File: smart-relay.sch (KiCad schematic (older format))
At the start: 16 parts, among them IC1 TMCS1101A4BQDR, J1 Screw_Terminal_01x03, J2 Conn_01x04, K1 G5LE-1, Q1 BSS138K, U1 OPAMP, U2 ATtiny85-20PU

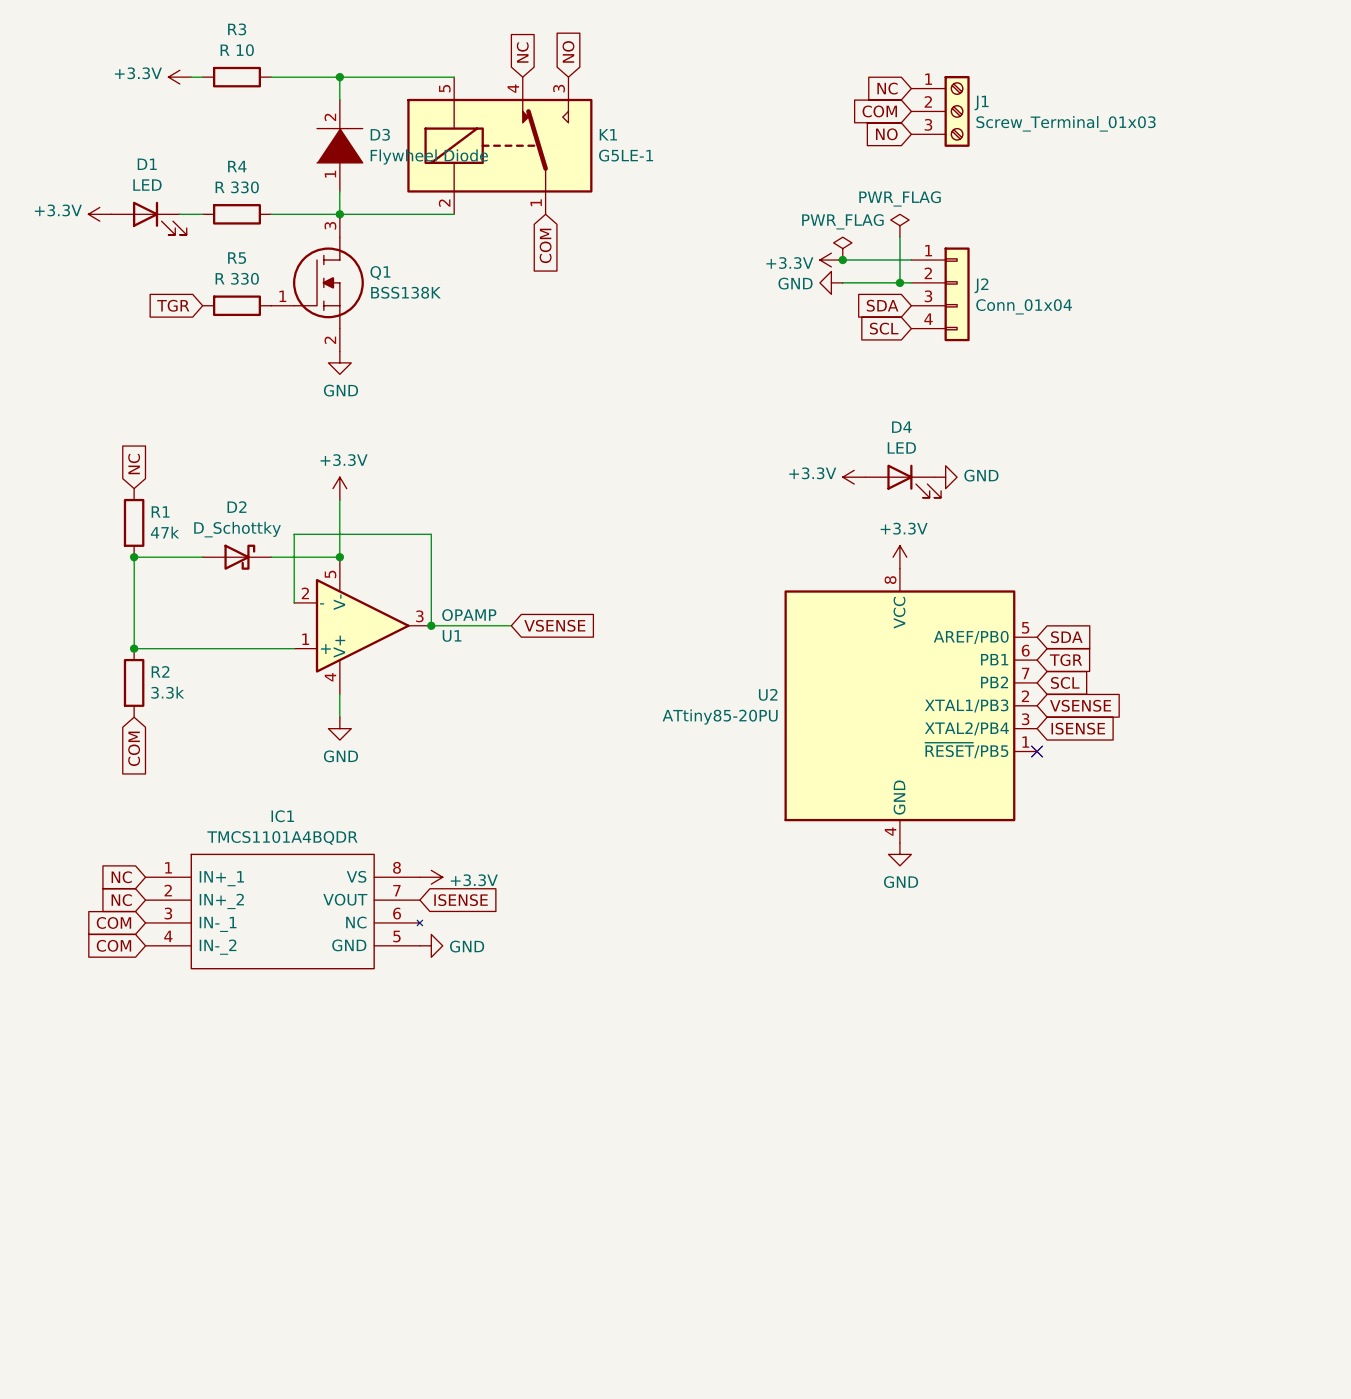
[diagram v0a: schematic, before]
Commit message: add decoupling cap and headers
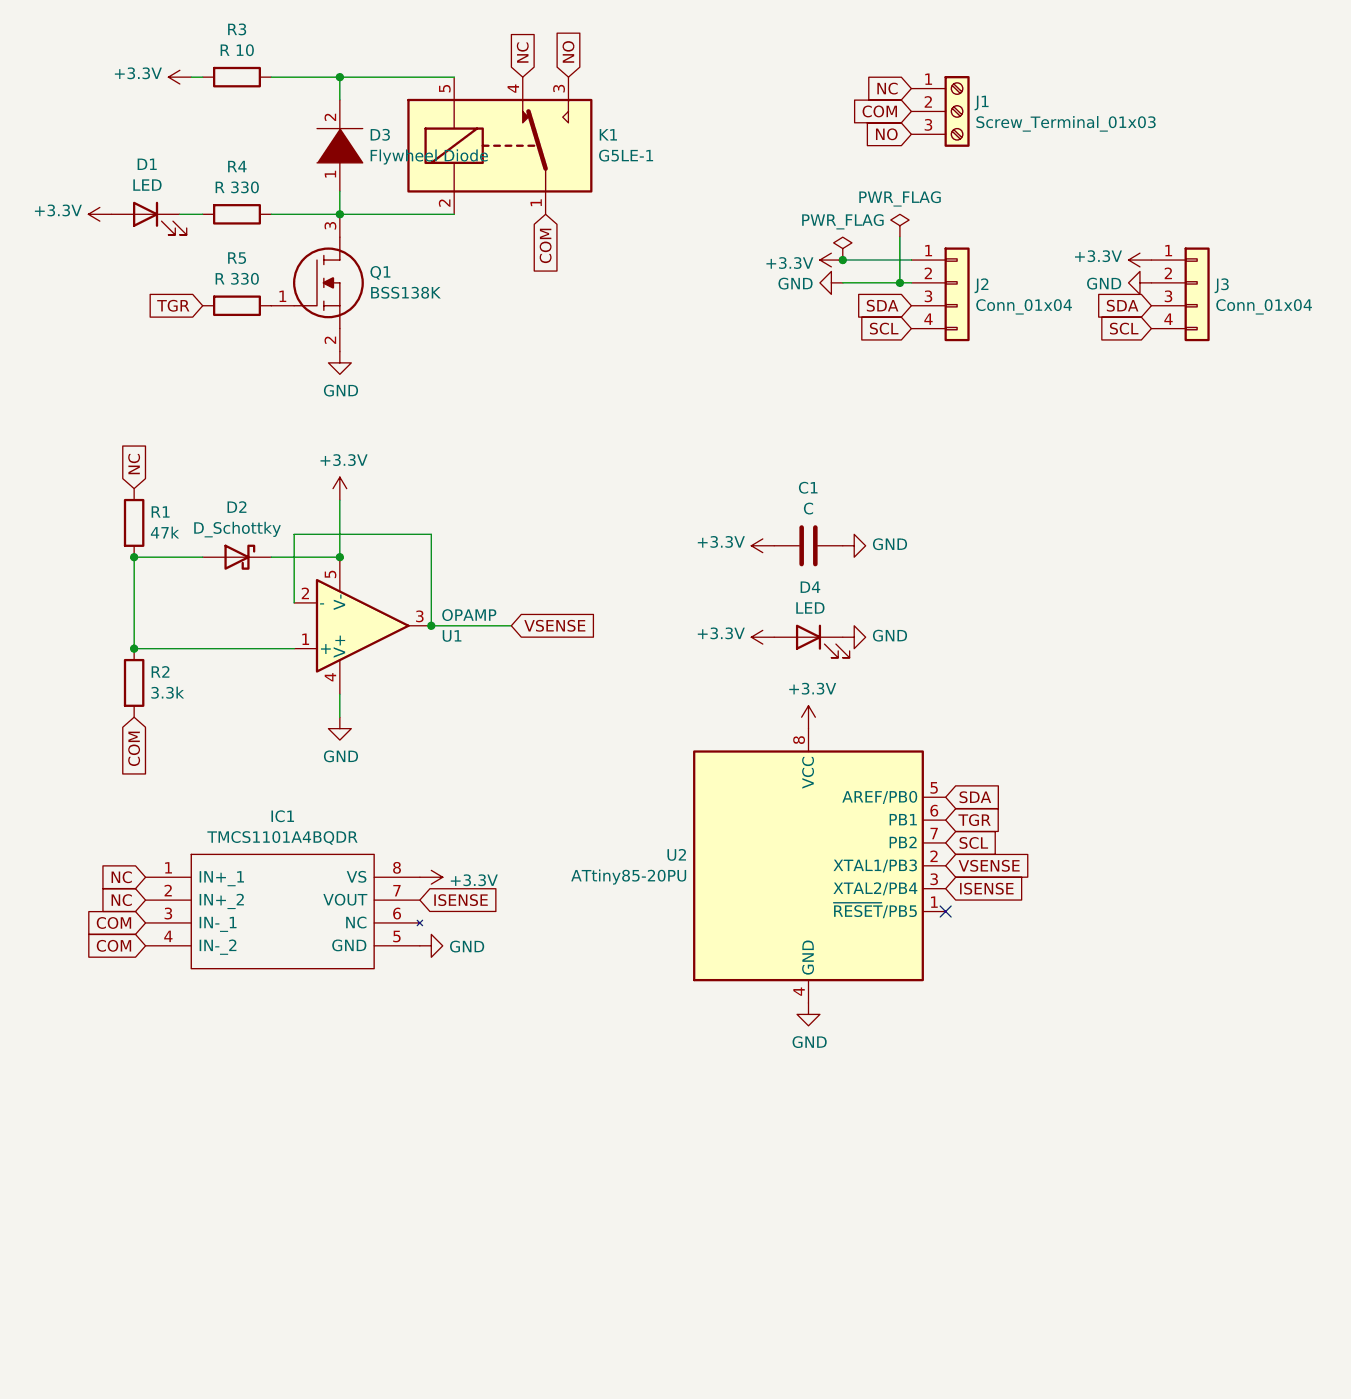
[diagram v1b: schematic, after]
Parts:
- added C1: C, smart-relay:K104K15X7RF53H5, symbol Device:C
- added J3: Conn_01x04, Connector_PinHeader_2.54mm:PinHeader_1x04_P2.54mm_Vertical, symbol Connector_Generic:Conn_01x04
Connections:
- net +3V3: now also C1.2, J3.1 (Pin_1)
- net GND: now also C1.1, J3.2 (Pin_2)
- net SCL: now also J3.4 (Pin_4)
- net SDA: now also J3.3 (Pin_3)
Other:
- moved on the sheet: D4, U2
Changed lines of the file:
@@
 Text GLabel 1100 3650 3    50   Input ~ 0
 COM
-Text GLabel 5050 3300 2    50   Input ~ 0
+Text GLabel 4650 4000 2    50   Input ~ 0
 SDA
-Text GLabel 5050 3500 2    50   Input ~ 0
+Text GLabel 4650 4200 2    50   Input ~ 0
 SCL
-Text GLabel 5050 3600 2    50   Input ~ 0
+Text GLabel 4650 4300 2    50   Input ~ 0
 VSENSE
-NoConn ~ 5050 3800
+NoConn ~ 4650 4500
 $Comp
 L power:PWR_FLAG #FLG0102
@@
 L MCU_Microchip_ATtiny:ATtiny85-20PU U2
 U 1 1 5FA464BB
-P 4450 3600
-F 0 "U2" H 3921 3646 50  0000 R CNN
-F 1 "ATtiny85-20PU" H 3921 3555 50  0000 R CNN
-F 2 "Package_DIP:DIP-8_W7.62mm" H 4450 3600 50  0001 C CIN
-F 3 "http://ww1.microchip.com/downloads/en/DeviceDoc/atmel-2586-avr-8-bit-microcontroller-attiny25-attiny45-attiny85_datasheet.pdf" H 4450 3600 50  0001 C CNN
-	1    4450 3600
+P 4050 4300
+F 0 "U2" H 3521 4346 50  0000 R CNN
+F 1 "ATtiny85-20PU" H 3521 4255 50  0000 R CNN
+F 2 "Package_DIP:DIP-8_W7.62mm" H 4050 4300 50  0001 C CIN
+F 3 "http://ww1.microchip.com/downloads/en/DeviceDoc/atmel-2586-avr-8-bit-microcontroller-attiny25-attiny45-attiny85_datasheet.pdf" H 4050 4300 50  0001 C CNN
+	1    4050 4300
 	1    0    0    -1
 $EndComp
@@
 Wire Wire Line
 	4450 1550 4450 1750
-Text GLabel 5050 3400 2    50   Input ~ 0
+Text GLabel 4650 4100 2    50   Input ~ 0
 TGR
 $Comp
@@
 L power:GND #PWR09
 U 1 1 5FC4B5B3
-P 4450 4200
-F 0 "#PWR09" H 4450 3950 50  0001 C CNN
-F 1 "GND" H 4455 4027 50  0000 C CNN
-F 2 "" H 4450 4200 50  0001 C CNN
-F 3 "" H 4450 4200 50  0001 C CNN
-	1    4450 4200
+P 4050 4900
+F 0 "#PWR09" H 4050 4650 50  0001 C CNN
+F 1 "GND" H 4055 4727 50  0000 C CNN
+F 2 "" H 4050 4900 50  0001 C CNN
+F 3 "" H 4050 4900 50  0001 C CNN
+	1    4050 4900
 	1    0    0    -1
 $EndComp
@@
 L power:+3.3V #PWR0104
 U 1 1 5FCB6B03
-P 4450 3000
-F 0 "#PWR0104" H 4450 2850 50  0001 C CNN
-F 1 "+3.3V" H 4465 3173 50  0000 C CNN
-F 2 "" H 4450 3000 50  0001 C CNN
-F 3 "" H 4450 3000 50  0001 C CNN
-	1    4450 3000
+P 4050 3700
+F 0 "#PWR0104" H 4050 3550 50  0001 C CNN
+F 1 "+3.3V" H 4065 3873 50  0000 C CNN
+F 2 "" H 4050 3700 50  0001 C CNN
+F 3 "" H 4050 3700 50  0001 C CNN
+	1    4050 3700
 	1    0    0    -1
 $EndComp
@@
 L Device:LED D4
 U 1 1 5FCCB65C
-P 4450 2600
-F 0 "D4" H 4443 2817 50  0000 C CNN
-F 1 "LED" H 4443 2726 50  0000 C CNN
-F 2 "smart-relay:LTL4232" H 4450 2600 50  0001 C CNN
-F 3 "~" H 4450 2600 50  0001 C CNN
-	1    4450 2600
+P 4050 3300
+F 0 "D4" H 4043 3517 50  0000 C CNN
+F 1 "LED" H 4043 3426 50  0000 C CNN
+F 2 "smart-relay:LTL4232" H 4050 3300 50  0001 C CNN
+F 3 "~" H 4050 3300 50  0001 C CNN
+	1    4050 3300
 	-1   0    0    -1
 $EndComp
@@
 L power:+3.3V #PWR06
 U 1 1 5FCCB662
-P 4300 2600
-F 0 "#PWR06" H 4300 2450 50  0001 C CNN
-F 1 "+3.3V" V 4315 2728 50  0000 L CNN
-F 2 "" H 4300 2600 50  0001 C CNN
-F 3 "" H 4300 2600 50  0001 C CNN
-	1    4300 2600
+P 3900 3300
+F 0 "#PWR06" H 3900 3150 50  0001 C CNN
+F 1 "+3.3V" V 3915 3428 50  0000 L CNN
+F 2 "" H 3900 3300 50  0001 C CNN
+F 3 "" H 3900 3300 50  0001 C CNN
+	1    3900 3300
 	0    -1   -1   0
 $EndComp
@@
 L power:GND #PWR08
 U 1 1 5FCD4BB4
-P 4600 2600
-F 0 "#PWR08" H 4600 2350 50  0001 C CNN
-F 1 "GND" V 4605 2472 50  0000 R CNN
-F 2 "" H 4600 2600 50  0001 C CNN
-F 3 "" H 4600 2600 50  0001 C CNN
-	1    4600 2600
+P 4200 3300
+F 0 "#PWR08" H 4200 3050 50  0001 C CNN
+F 1 "GND" V 4205 3172 50  0000 R CNN
+F 2 "" H 4200 3300 50  0001 C CNN
+F 3 "" H 4200 3300 50  0001 C CNN
+	1    4200 3300
 	0    -1   -1   0
 $EndComp
@@
 Text GLabel 1150 4350 0    50   Input ~ 0
 NC
-Text GLabel 5050 3700 2    50   Input ~ 0
+Text GLabel 4650 4400 2    50   Input ~ 0
 ISENSE
 Text GLabel 2350 4450 2    50   Input ~ 0
 ISENSE
+$Comp
+L Connector_Generic:Conn_01x04 J3
+U 1 1 5FC40FD3
+P 5750 1750
+F 0 "J3" H 5830 1742 50  0000 L CNN
+F 1 "Conn_01x04" H 5830 1651 50  0000 L CNN
+F 2 "Connector_PinHeader_2.54mm:PinHeader_1x04_P2.54mm_Vertical" H 5750 1750 50  0001 C CNN
+F 3 "~" H 5750 1750 50  0001 C CNN
+	1    5750 1750
+	1    0    0    -1
+$EndComp
+Text GLabel 5550 1950 0    50   Input ~ 0
+SCL
+Text GLabel 5550 1850 0    50   Input ~ 0
+SDA
+$Comp
+L power:GND #PWR0106
+U 1 1 5FC44121
+P 5550 1750
+F 0 "#PWR0106" H 5550 1500 50  0001 C CNN
+F 1 "GND" V 5555 1622 50  0000 R CNN
+F 2 "" H 5550 1750 50  0001 C CNN
+F 3 "" H 5550 1750 50  0001 C CNN
+	1    5550 1750
+	0    1    1    0
+$EndComp
+$Comp
+L power:+3.3V #PWR0107
+U 1 1 5FC467E9
+P 5550 1650
+F 0 "#PWR0107" H 5550 1500 50  0001 C CNN
+F 1 "+3.3V" V 5565 1778 50  0000 L CNN
+F 2 "" H 5550 1650 50  0001 C CNN
+F 3 "" H 5550 1650 50  0001 C CNN
+	1    5550 1650
+	0    -1   -1   0
+$EndComp
+$Comp
+L Device:C C1
+U 1 1 5FC51BF5
+P 4050 2900
+F 0 "C1" V 3798 2900 50  0000 C CNN
+F 1 "C" V 3889 2900 50  0000 C CNN
+F 2 "smart-relay:K104K15X7RF53H5" H 4088 2750 50  0001 C CNN
+F 3 "~" H 4050 2900 50  0001 C CNN
+	1    4050 2900
+	0    1    1    0
+$EndComp
+$Comp
+L power:+3.3V #PWR02
+U 1 1 5FC54F6B
+P 3900 2900
+F 0 "#PWR02" H 3900 2750 50  0001 C CNN
+F 1 "+3.3V" V 3915 3028 50  0000 L CNN
+F 2 "" H 3900 2900 50  0001 C CNN
+F 3 "" H 3900 2900 50  0001 C CNN
+	1    3900 2900
+	0    -1   -1   0
+$EndComp
+$Comp
+L power:GND #PWR010
+U 1 1 5FC56C31
+P 4200 2900
+F 0 "#PWR010" H 4200 2650 50  0001 C CNN
+F 1 "GND" V 4205 2772 50  0000 R CNN
+F 2 "" H 4200 2900 50  0001 C CNN
+F 3 "" H 4200 2900 50  0001 C CNN
+	1    4200 2900
+	0    -1   -1   0
+$EndComp
 $EndSCHEMATC

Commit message: add another voltage sensor
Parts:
- added D?: D_Schottky, smart-relay:DIO_1N4447, symbol Device:D_Schottky
- added R?: 3.3k, Resistor_THT:R_Axial_DIN0204_L3.6mm_D1.6mm_P1.90mm_Vertical, symbol Device:R
- added R?: 47k, Resistor_THT:R_Axial_DIN0204_L3.6mm_D1.6mm_P1.90mm_Vertical, symbol Device:R
- added R?: R 330, Resistor_THT:R_Axial_DIN0204_L3.6mm_D1.6mm_P1.90mm_Vertical, symbol Device:R
- added U?: OPAMP, smart-relay:SOT95P280X145-5N, symbol pspice:OPAMP
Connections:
- net +3V3: now also D?.1 (K), U?.5 (V-)
- net COM: now also R?.2
- net GND: now also R?.1, U?.4 (V+); no longer D4.1 (K)
- net NO: now also R?.1
- net VSENSE2: now reaches U2.1 (~RESET~/PB5)
- net VSENSE2: now also U?.2 (-), U?.3
- net VSENSE renamed VSENSE1
- new net: D4.1 (K), R?.2
- new net: D?.2 (A), R?.1, R?.2, U?.1 (+)
- no-connect marks 1 -> 0
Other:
- moved on the sheet: IC1
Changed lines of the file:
@@
 $EndComp
 Text GLabel 2750 3250 2    50   Input ~ 0
-VSENSE
+VSENSE1
 Wire Wire Line
 	2750 3250 2400 3250
@@
 SCL
 Text GLabel 4650 4300 2    50   Input ~ 0
-VSENSE
-NoConn ~ 4650 4500
+VSENSE1
 $Comp
 L power:PWR_FLAG #FLG0102
@@
 L power:GND #PWR08
 U 1 1 5FCD4BB4
-P 4200 3300
-F 0 "#PWR08" H 4200 3050 50  0001 C CNN
-F 1 "GND" V 4205 3172 50  0000 R CNN
-F 2 "" H 4200 3300 50  0001 C CNN
-F 3 "" H 4200 3300 50  0001 C CNN
-	1    4200 3300
+P 4500 3300
+F 0 "#PWR08" H 4500 3050 50  0001 C CNN
+F 1 "GND" V 4505 3172 50  0000 R CNN
+F 2 "" H 4500 3300 50  0001 C CNN
+F 3 "" H 4500 3300 50  0001 C CNN
+	1    4500 3300
 	0    -1   -1   0
 $EndComp
@@
 L smart-relay:TMCS1101A4BQDR IC1
 U 1 1 5FCE5121
-P 1150 4350
-F 0 "IC1" H 1750 4615 50  0000 C CNN
-F 1 "TMCS1101A4BQDR" H 1750 4524 50  0000 C CNN
-F 2 "smart-relay:SOIC127P600X175-8N" H 2200 4450 50  0001 L CNN
-F 3 "https://www.ti.com/lit/ds/symlink/tmcs1101.pdf?ts=1600726579455&ref_url=https%253A%252F%252Fwww.ti.com%252Fstore%252Fti%252Fen%252Fp%252Fproduct%252F%253Fp%253DTMCS1101A4BQDR" H 2200 4350 50  0001 L CNN
-F 4 "Board Mount Hall Effect / Magnetic Sensors Precision isolated current sensor with internal reference" H 2200 4250 50  0001 L CNN "Description"
-F 5 "1.75" H 2200 4150 50  0001 L CNN "Height"
-F 6 "Texas Instruments" H 2200 4050 50  0001 L CNN "Manufacturer_Name"
-F 7 "TMCS1101A4BQDR" H 2200 3950 50  0001 L CNN "Manufacturer_Part_Number"
-F 8 "595-TMCS1101A4BQDR" H 2200 3650 50  0001 L CNN "Mouser Part Number"
-F 9 "https://www.mouser.co.uk/ProductDetail/Texas-Instruments/TMCS1101A4BQDR?qs=7MVldsJ5Uazdi4bfyl50vQ%3D%3D" H 2200 3550 50  0001 L CNN "Mouser Price/Stock"
-	1    1150 4350
+P 1000 6150
+F 0 "IC1" H 1600 6415 50  0000 C CNN
+F 1 "TMCS1101A4BQDR" H 1600 6324 50  0000 C CNN
+F 2 "smart-relay:SOIC127P600X175-8N" H 2050 6250 50  0001 L CNN
+F 3 "https://www.ti.com/lit/ds/symlink/tmcs1101.pdf?ts=1600726579455&ref_url=https%253A%252F%252Fwww.ti.com%252Fstore%252Fti%252Fen%252Fp%252Fproduct%252F%253Fp%253DTMCS1101A4BQDR" H 2050 6150 50  0001 L CNN
+F 4 "Board Mount Hall Effect / Magnetic Sensors Precision isolated current sensor with internal reference" H 2050 6050 50  0001 L CNN "Description"
+F 5 "1.75" H 2050 5950 50  0001 L CNN "Height"
+F 6 "Texas Instruments" H 2050 5850 50  0001 L CNN "Manufacturer_Name"
+F 7 "TMCS1101A4BQDR" H 2050 5750 50  0001 L CNN "Manufacturer_Part_Number"
+F 8 "595-TMCS1101A4BQDR" H 2050 5450 50  0001 L CNN "Mouser Part Number"
+F 9 "https://www.mouser.co.uk/ProductDetail/Texas-Instruments/TMCS1101A4BQDR?qs=7MVldsJ5Uazdi4bfyl50vQ%3D%3D" H 2050 5350 50  0001 L CNN "Mouser Price/Stock"
+	1    1000 6150
 	1    0    0    -1
 $EndComp
@@
 L power:+3.3V #PWR01
 U 1 1 5FCE5CF5
-P 2350 4350
-F 0 "#PWR01" H 2350 4200 50  0001 C CNN
-F 1 "+3.3V" V 2365 4478 50  0000 L CNN
-F 2 "" H 2350 4350 50  0001 C CNN
-F 3 "" H 2350 4350 50  0001 C CNN
-	1    2350 4350
+P 2200 6150
+F 0 "#PWR01" H 2200 6000 50  0001 C CNN
+F 1 "+3.3V" V 2215 6278 50  0000 L CNN
+F 2 "" H 2200 6150 50  0001 C CNN
+F 3 "" H 2200 6150 50  0001 C CNN
+	1    2200 6150
 	0    1    1    0
 $EndComp
@@
 L power:GND #PWR04
 U 1 1 5FCE9249
-P 2350 4650
-F 0 "#PWR04" H 2350 4400 50  0001 C CNN
-F 1 "GND" V 2355 4522 50  0000 R CNN
-F 2 "" H 2350 4650 50  0001 C CNN
-F 3 "" H 2350 4650 50  0001 C CNN
-	1    2350 4650
+P 2200 6450
+F 0 "#PWR04" H 2200 6200 50  0001 C CNN
+F 1 "GND" V 2205 6322 50  0000 R CNN
+F 2 "" H 2200 6450 50  0001 C CNN
+F 3 "" H 2200 6450 50  0001 C CNN
+	1    2200 6450
 	0    -1   1    0
 $EndComp
-Text GLabel 1150 4650 0    50   Input ~ 0
+Text GLabel 1000 6450 0    50   Input ~ 0
 COM
-Text GLabel 1150 4550 0    50   Input ~ 0
+Text GLabel 1000 6350 0    50   Input ~ 0
 COM
-Text GLabel 1150 4450 0    50   Input ~ 0
+Text GLabel 1000 6250 0    50   Input ~ 0
 NC
-Text GLabel 1150 4350 0    50   Input ~ 0
+Text GLabel 1000 6150 0    50   Input ~ 0
 NC
 Text GLabel 4650 4400 2    50   Input ~ 0
 ISENSE
-Text GLabel 2350 4450 2    50   Input ~ 0
+Text GLabel 2200 6250 2    50   Input ~ 0
 ISENSE
 $Comp
@@
 	0    -1   -1   0
 $EndComp
+Text GLabel 2750 4900 2    50   Input ~ 0
+VSENSE2
+Wire Wire Line
+	2750 4900 2400 4900
+$Comp
+L pspice:OPAMP U?
+U 1 1 5FDAA562
+P 2100 4900
+F 0 "U?" H 2444 4946 50  0000 L CNN
+F 1 "OPAMP" H 2444 4855 50  0000 L CNN
+F 2 "smart-relay:SOT95P280X145-5N" H 2100 4900 50  0001 C CNN
+F 3 "~" H 2100 4900 50  0001 C CNN
+	1    2100 4900
+	1    0    0    1
+$EndComp
+$Comp
+L Device:R R?
+U 1 1 5FDAA568
+P 1100 5150
+F 0 "R?" H 1170 5196 50  0000 L CNN
+F 1 "3.3k" H 1170 5105 50  0000 L CNN
+F 2 "Resistor_THT:R_Axial_DIN0204_L3.6mm_D1.6mm_P1.90mm_Vertical" V 1030 5150 50  0001 C CNN
+F 3 "~" H 1100 5150 50  0001 C CNN
+	1    1100 5150
+	1    0    0    -1
+$EndComp
+$Comp
+L Device:R R?
+U 1 1 5FDAA56E
+P 1100 4450
+F 0 "R?" H 1170 4496 50  0000 L CNN
+F 1 "47k" H 1170 4405 50  0000 L CNN
+F 2 "Resistor_THT:R_Axial_DIN0204_L3.6mm_D1.6mm_P1.90mm_Vertical" V 1030 4450 50  0001 C CNN
+F 3 "~" H 1100 4450 50  0001 C CNN
+	1    1100 4450
+	1    0    0    -1
+$EndComp
+Text GLabel 1100 4300 1    50   Input ~ 0
+NO
+Wire Wire Line
+	1100 4600 1100 5000
+$Comp
+L Device:D_Schottky D?
+U 1 1 5FDAA576
+P 1550 4600
+F 0 "D?" H 1550 4817 50  0000 C CNN
+F 1 "D_Schottky" H 1550 4726 50  0000 C CNN
+F 2 "smart-relay:DIO_1N4447" H 1550 4600 50  0001 C CNN
+F 3 "~" H 1550 4600 50  0001 C CNN
+	1    1550 4600
+	-1   0    0    -1
+$EndComp
+Wire Wire Line
+	1400 4600 1100 4600
+Connection ~ 1100 4600
+Wire Wire Line
+	1700 4600 2000 4600
+Connection ~ 2000 4600
+Wire Wire Line
+	2000 4350 2000 4600
+Wire Wire Line
+	2400 4900 2400 4500
+Wire Wire Line
+	2400 4500 1800 4500
+Wire Wire Line
+	1800 4500 1800 4800
+Connection ~ 2400 4900
+Wire Wire Line
+	1800 5000 1100 5000
+Connection ~ 1100 5000
+Wire Wire Line
+	2000 5200 2000 5300
+Text GLabel 1100 5300 3    50   Input ~ 0
+COM
+$Comp
+L power:GND #PWR?
+U 1 1 5FDAA589
+P 2000 5300
+F 0 "#PWR?" H 2000 5050 50  0001 C CNN
+F 1 "GND" H 2005 5127 50  0000 C CNN
+F 2 "" H 2000 5300 50  0001 C CNN
+F 3 "" H 2000 5300 50  0001 C CNN
+	1    2000 5300
+	1    0    0    -1
+$EndComp
+$Comp
+L power:+3.3V #PWR?
+U 1 1 5FDAA58F
+P 2000 4350
+F 0 "#PWR?" H 2000 4200 50  0001 C CNN
+F 1 "+3.3V" H 2015 4523 50  0000 C CNN
+F 2 "" H 2000 4350 50  0001 C CNN
+F 3 "" H 2000 4350 50  0001 C CNN
+	1    2000 4350
+	1    0    0    -1
+$EndComp
+Text GLabel 4650 4500 2    50   Input ~ 0
+VSENSE2
+$Comp
+L Device:R R?
+U 1 1 5FDBEB46
+P 4350 3300
+F 0 "R?" V 4143 3300 50  0000 C CNN
+F 1 "R 330" V 4234 3300 50  0000 C CNN
+F 2 "Resistor_THT:R_Axial_DIN0204_L3.6mm_D1.6mm_P1.90mm_Vertical" V 4280 3300 50  0001 C CNN
+F 3 "~" H 4350 3300 50  0001 C CNN
+	1    4350 3300
+	0    1    1    0
+$EndComp
 $EndSCHEMATC
